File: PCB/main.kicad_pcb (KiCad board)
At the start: 4 copper layers, 65.2 x 45.1 mm, 64 parts, among them J1 S20B-PADSS-1, J2 S20B-PADSS-1, J3 SWD, SW1 SPST, U1 XC6206P33, U3 MCP2558FD, U4 MCP2558FD, U5 STM32G0B1, U6 TPS54302, Y1 40M

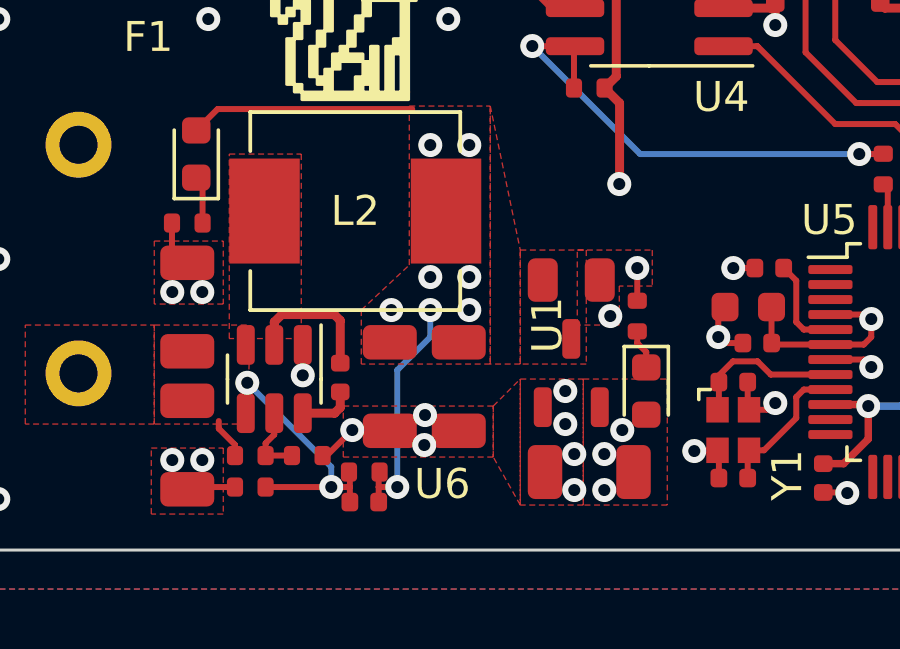
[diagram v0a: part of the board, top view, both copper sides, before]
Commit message: Switch to TJA1051T/3
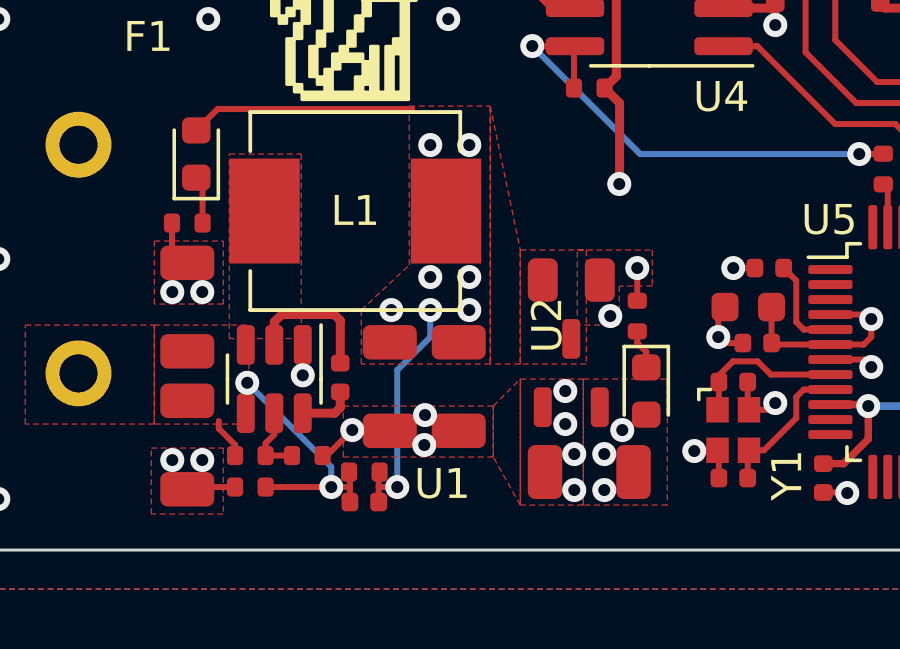
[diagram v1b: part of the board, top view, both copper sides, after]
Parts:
- U3, U4: value MCP2558FD -> TJA1051T/3
- renumbered C20 to C1, C11 to C10, C12 to C11, C13 to C12, C18 to C13, C17 to C14, C19 to C15, C14 to C16, C15 to C17, C16 to C18, C22 to C2, C23 to C3, C24 to C4, C25 to C5, C26 to C6, C1 to C7, C2 to C8, C10 to C9, D5 to D1, D1 to D2, D4 to D3, L2 to L1, R16 to R1, R8 to R10, R9 to R11, R10 to R12, R11 to R13, R13 to R14, R21 to R15, R22 to R16, R15 to R17, R17 to R18, R12 to R19, R18 to R2, R14 to R20, R25 to R21, R26 to R22, R27 to R25, R28 to R3, R20 to R4, R19 to R5, R1 to R6, R5 to R7, R6 to R8, R7 to R9, U6 to U1, U1 to U2

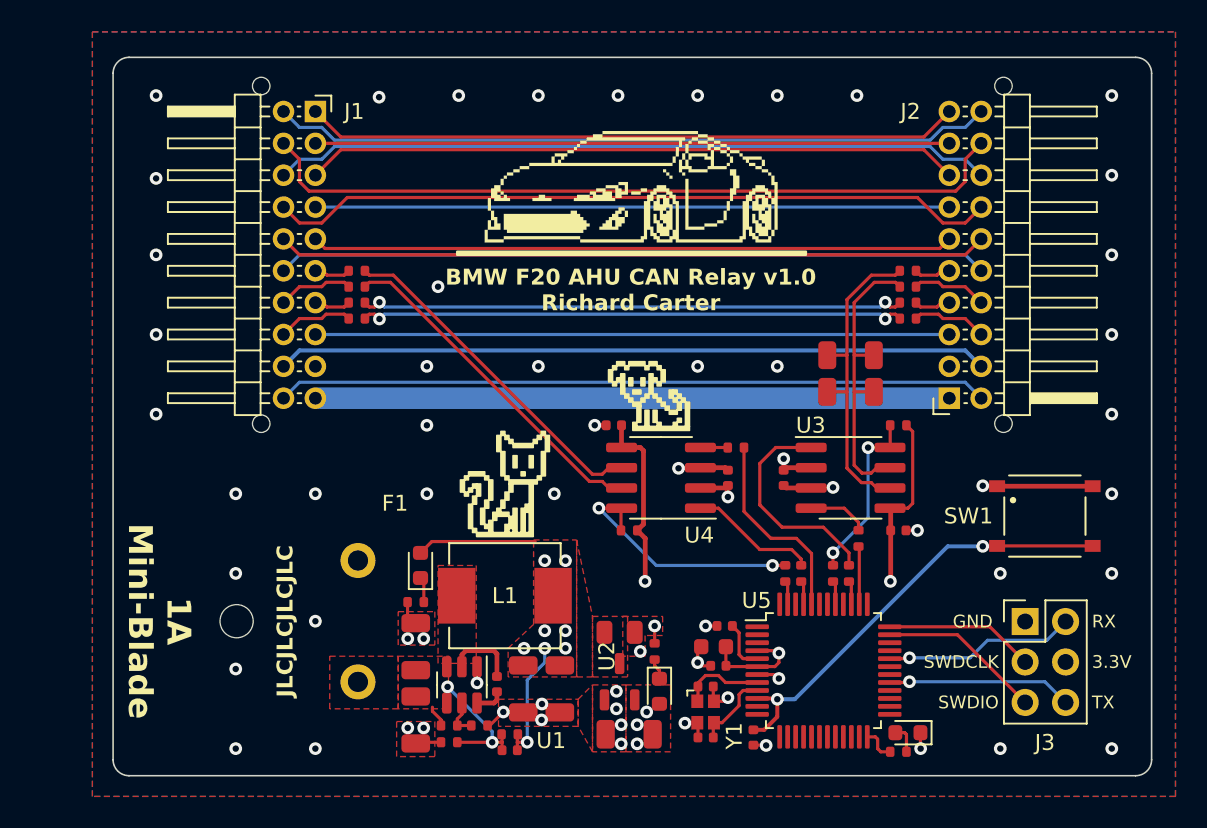
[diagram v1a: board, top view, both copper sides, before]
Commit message: Added bulk capacitance
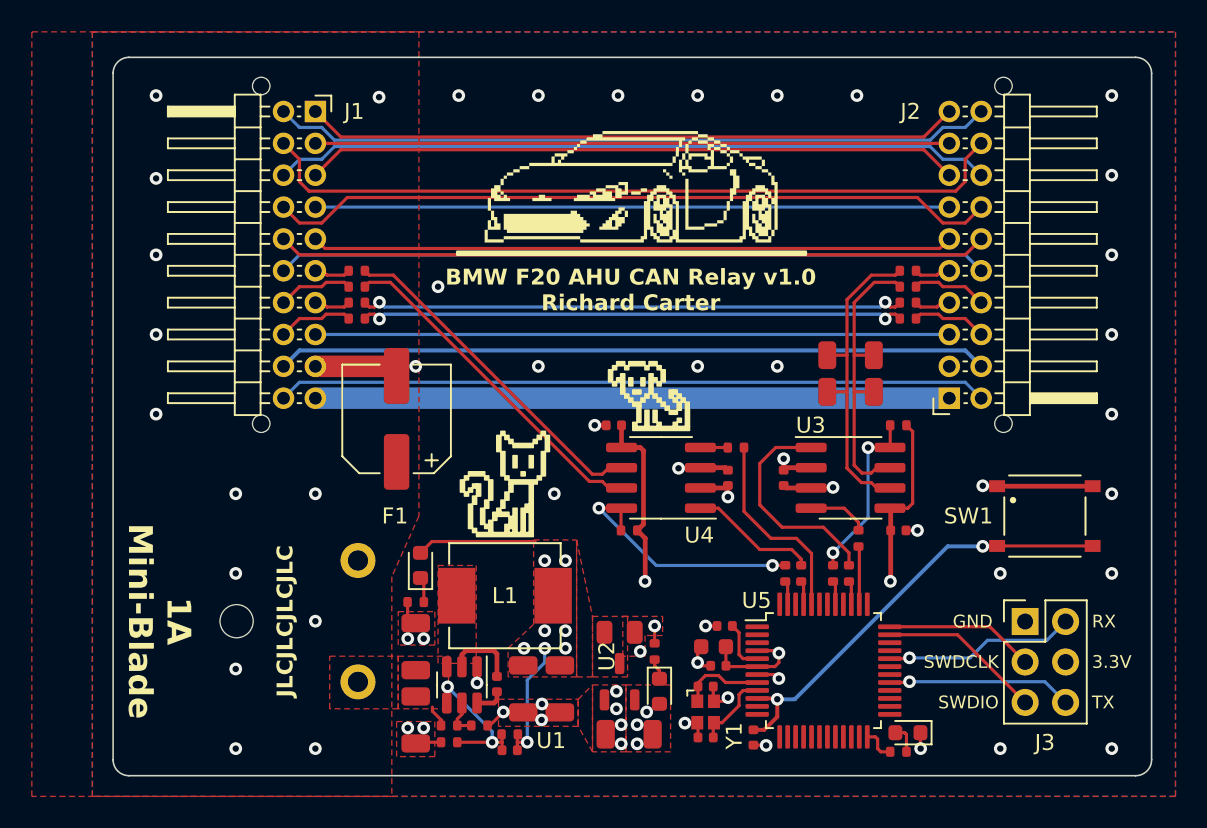
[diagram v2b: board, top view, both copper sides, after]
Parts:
- added C19: 47u, Capacitor_SMD:CP_Elec_6.3x5.8, F.Cu at (45.1, 49.3)
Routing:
- net GND: track 29.7 -> 34.9 mm, vias 63 -> 61
- added copper zone on F.Cu, net /JST_10_BAT+
- removed copper zone on In2.Cu, net /JST_10_BAT+
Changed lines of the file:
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@@
     )
   )
+  (footprint "Capacitor_SMD:CP_Elec_6.3x5.8" (layer "F.Cu")
+    (at 45.1 49.3 90)
+    (descr "SMD capacitor, aluminum electrolytic, Nichicon, 6.3x5.8mm")
+    (tags "capacitor electrolytic")
+    (property "Capacitance" "47u")
+    (property "Capacitance Tolerance" "20%")
+    (property "Case Package Size" "6.3x5.8 mm")
+    (property "Dielectric" "Aluminium")
+    (property "LCSC" "LCSC: C178545")
+    (property "MPN" "EEE-FK1E470P")
+    (property "Manufacturer" "Panasonic")
+    (property "Sheetfile" "main.kicad_sch")
+    (property "Sheetname" "")
+    (property "Voltage Rating" "25V")
+    (property "ki_description" "CAP ALUM 47UF 20% 25V SMD")
+    (property "ki_keywords" "cap capacitor")
+    (attr smd)
+    (fp_text reference "C19" (at 0 -4.35 90) (layer "F.SilkS") hide
+        (effects (font (size 1 1) (thickness 0.15)))
+    )
+    (fp_text value "47u" (at 0 4.35 90) (layer "F.Fab")
+        (effects (font (size 1 1) (thickness 0.15)))
+    )
+    (fp_text user "${REFERENCE}" (at 0 0 90) (layer "F.Fab")
+        (effects (font (size 1 1) (thickness 0.15)))
+    )
+    (fp_line (start -3.41 -2.345563) (end -3.41 -1.06)
+      (stroke (width 0.12) (type solid)) (layer "F.SilkS"))
+    (fp_line (start -3.41 -2.345563) (end -2.345563 -3.41)
+      (stroke (width 0.12) (type solid)) (layer "F.SilkS"))
+    (fp_line (start -3.41 2.345563) (end -3.41 1.06)
+      (stroke (width 0.12) (type solid)) (layer "F.SilkS"))
+    (fp_line (start -3.41 2.345563) (end -2.345563 3.41)
+      (stroke (width 0.12) (type solid)) (layer "F.SilkS"))
+    (fp_line (start -2.99375 2.2) (end -2.20625 2.2)
+      (stroke (width 0.12) (type solid)) (layer "F.SilkS"))
+    (fp_line (start -2.6 1.80625) (end -2.6 2.59375)
+      (stroke (width 0.12) (type solid)) (layer "F.SilkS"))
+    (fp_line (start -2.345563 -3.41) (end 3.41 -3.41)
+      (stroke (width 0.12) (type solid)) (layer "F.SilkS"))
+    (fp_line (start -2.345563 3.41) (end 3.41 3.41)
+      (stroke (width 0.12) (type solid)) (layer "F.SilkS"))
+    (fp_line (start 3.41 -3.41) (end 3.41 -1.06)
+      (stroke (width 0.12) (type solid)) (layer "F.SilkS"))
+    (fp_line (start 3.41 3.41) (end 3.41 1.06)
+      (stroke (width 0.12) (type solid)) (layer "F.SilkS"))
+    (fp_line (start -4.7 -1.05) (end -4.7 1.05)
+      (stroke (width 0.05) (type solid)) (layer "F.CrtYd"))
+    (fp_line (start -4.7 1.05) (end -3.55 1.05)
+      (stroke (width 0.05) (type solid)) (layer "F.CrtYd"))
+    (fp_line (start -3.55 -2.4) (end -3.55 -1.05)
+      (stroke (width 0.05) (type solid)) (layer "F.CrtYd"))
+    (fp_line (start -3.55 -2.4) (end -2.4 -3.55)
+      (stroke (width 0.05) (type solid)) (layer "F.CrtYd"))
+    (fp_line (start -3.55 -1.05) (end -4.7 -1.05)
+      (stroke (width 0.05) (type solid)) (layer "F.CrtYd"))
+    (fp_line (start -3.55 1.05) (end -3.55 2.4)
+      (stroke (width 0.05) (type solid)) (layer "F.CrtYd"))
+    (fp_line (start -3.55 2.4) (end -2.4 3.55)
+      (stroke (width 0.05) (type solid)) (layer "F.CrtYd"))
+    (fp_line (start -2.4 -3.55) (end 3.55 -3.55)
+      (stroke (width 0.05) (type solid)) (layer "F.CrtYd"))
+    (fp_line (start -2.4 3.55) (end 3.55 3.55)
+      (stroke (width 0.05) (type solid)) (layer "F.CrtYd"))
+    (fp_line (start 3.55 -3.55) (end 3.55 -1.05)
+      (stroke (width 0.05) (type solid)) (layer "F.CrtYd"))
+    (fp_line (start 3.55 -1.05) (end 4.7 -1.05)
+      (stroke (width 0.05) (type solid)) (layer "F.CrtYd"))
+    (fp_line (start 3.55 1.05) (end 3.55 3.55)
+      (stroke (width 0.05) (type solid)) (layer "F.CrtYd"))
+    (fp_line (start 4.7 -1.05) (end 4.7 1.05)
+      (stroke (width 0.05) (type solid)) (layer "F.CrtYd"))
+    (fp_line (start 4.7 1.05) (end 3.55 1.05)
+      (stroke (width 0.05) (type solid)) (layer "F.CrtYd"))
+    (fp_line (start -3.3 -2.3) (end -3.3 2.3)
+      (stroke (width 0.1) (type solid)) (layer "F.Fab"))
+    (fp_line (start -3.3 -2.3) (end -2.3 -3.3)
+      (stroke (width 0.1) (type solid)) (layer "F.Fab"))
+    (fp_line (start -3.3 2.3) (end -2.3 3.3)
+      (stroke (width 0.1) (type solid)) (layer "F.Fab"))
+    (fp_line (start -2.704838 -1.33) (end -2.074838 -1.33)
+      (stroke (width 0.1) (type solid)) (layer "F.Fab"))
+    (fp_line (start -2.389838 -1.645) (end -2.389838 -1.015)
+      (stroke (width 0.1) (type solid)) (layer "F.Fab"))
+    (fp_line (start -2.3 -3.3) (end 3.3 -3.3)
+      (stroke (width 0.1) (type solid)) (layer "F.Fab"))
+    (fp_line (start -2.3 3.3) (end 3.3 3.3)
+      (stroke (width 0.1) (type solid)) (layer "F.Fab"))
+    (fp_line (start 3.3 -3.3) (end 3.3 3.3)
+      (stroke (width 0.1) (type solid)) (layer "F.Fab"))
+    (fp_circle (center 0 0) (end 3.15 0)
+      (stroke (width 0.1) (type solid)) (fill none) (layer "F.Fab"))
+    (pad "1" smd roundrect (at -2.7 0 90) (size 3.5 1.6) (layers "F.Cu" "F.Paste" "F.Mask") (roundrect_rratio 0.15625)
+      (net 61 "/JST_10_BAT+") (pintype "passive"))
+    (pad "2" smd roundrect (at 2.7 0 90) (size 3.5 1.6) (layers "F.Cu" "F.Paste" "F.Mask") (roundrect_rratio 0.15625)
+      (net 81 "GND") (pintype "passive"))
+    (model "${KICAD6_3DMODEL_DIR}/Capacitor_SMD.3dshapes/CP_Elec_6.3x5.8.wrl"
+      (offset (xyz 0 0 0))
+      (scale (xyz 1 1 1))
+      (rotate (xyz 0 0 0))
+    )
+  )
   (footprint "Resistor_SMD:R_0402_1005Metric" (layer "F.Cu")
     (at 42.6 40 180)
@@
     (property "ki_keywords" "fuse")
     (attr through_hole)
-    (fp_text reference "F1" (at -7.4 -9.9451) (layer "F.SilkS")
+    (fp_text reference "F1" (at -6.6 -9.9451) (layer "F.SilkS")
         (effects (font (size 1 1) (thickness 0.15)))
     )
@@
   (segment (start 65.22 62.3) (end 64.5 62.3) (width 0.2) (layer "F.Cu") (net 81))
   (segment (start 64.2 64.8) (end 64 64.6) (width 0.2) (layer "F.Cu") (net 81))
+  (segment (start 40 46) (end 45.2 46) (width 1.35) (layer "F.Cu") (net 81))
   (segment (start 69.4 52.52) (end 69.4 51.8) (width 0.3) (layer "F.Cu") (net 81))
   (segment (start 47.89 69.6) (end 46.625 69.6) (width 0.2) (layer "F.Cu") (net 81))
@@
   (via (at 78 70) (size 0.8) (drill 0.4) (layers "F.Cu" "B.Cu") (net 81))
   (via (at 90 44) (size 0.8) (drill 0.4) (layers "F.Cu" "B.Cu") (net 81))
-  (via (at 47 46) (size 0.8) (drill 0.4) (layers "F.Cu" "B.Cu") (net 81))
   (via (at 55 54) (size 0.8) (drill 0.4) (layers "F.Cu" "B.Cu") (free) (net 81))
   (via (at 47.7 41) (size 0.8) (drill 0.4) (layers "F.Cu" "B.Cu") (net 81))
@@
   (via (at 83 59) (size 0.8) (drill 0.4) (layers "F.Cu" "B.Cu") (free) (net 81))
   (via (at 35 59) (size 0.8) (drill 0.4) (layers "F.Cu" "B.Cu") (free) (net 81))
-  (via (at 47 49.7) (size 0.8) (drill 0.4) (layers "F.Cu" "B.Cu") (net 81))
   (via (at 69.1 65.599503) (size 0.8) (drill 0.4) (layers "F.Cu" "B.Cu") (net 81))
   (via (at 68.3 69.7995) (size 0.8) (drill 0.4) (layers "F.Cu" "B.Cu") (net 81))
@@
   (via (at 30 44) (size 0.8) (drill 0.4) (layers "F.Cu" "B.Cu") (net 81))
   (via (at 77.8 56.3) (size 0.8) (drill 0.4) (layers "F.Cu" "B.Cu") (net 81))
+  (via (at 46.3 46) (size 0.8) (drill 0.4) (layers "F.Cu" "B.Cu") (free) (net 81))
   (via (at 74 29) (size 0.8) (drill 0.4) (layers "F.Cu" "B.Cu") (net 81))
   (via (at 90 54) (size 0.8) (drill 0.4) (layers "F.Cu" "B.Cu") (free) (net 81))
@@
   (via (at 69.4 51.8) (size 0.8) (drill 0.4) (layers "F.Cu" "B.Cu") (net 81))
   (via (at 59.2 69.7) (size 0.8) (drill 0.4) (layers "F.Cu" "B.Cu") (free) (net 81))
-  (via (at 47 54) (size 0.8) (drill 0.4) (layers "F.Cu" "B.Cu") (free) (net 81))
   (via (at 44 29.1) (size 0.8) (drill 0.4) (layers "F.Cu" "B.Cu") (net 81))
   (via (at 58.9 67.5) (size 0.8) (drill 0.4) (layers "F.Cu" "B.Cu") (free) (net 81))
@@
     )
   )
+  (zone (net 61) (net_name "/JST_10_BAT+") (layer "F.Cu") (hatch edge 0.5)
+    (priority 5)
+    (connect_pads yes (clearance 0.5))
+    (min_thickness 0.25) (filled_areas_thickness no)
+    (fill yes (thermal_gap 0.5) (thermal_bridge_width 0.5))
+    (polygon
+      (pts
+        (xy 46.5 55.4)
+        (xy 44.8 59.2)
+        (xy 44.8 73)
+        (xy 22.2 73)
+        (xy 22.2 25)
+        (xy 46.5 25)
+      )
+    )
+  )
   (zone (net 81) (net_name "GND") (layers "F.Cu" "In1.Cu" "In2.Cu" "B.Cu") (hatch edge 0.5)
     (connect_pads yes (clearance 0.5))
@@
     (polygon
       (pts
-        (xy 44.7 49)
+        (xy 44.7 49.1)
         (xy 92.2 49.1)
         (xy 92.2 71)
@@
       )
     )
-  )
-  (zone (net 61) (net_name "/JST_10_BAT+") (layer "In2.Cu") (hatch edge 0.5)
-    (priority 5)
-    (connect_pads yes (clearance 0.5))
-    (min_thickness 0.25) (filled_areas_thickness no)
-    (fill yes (thermal_gap 0.5) (thermal_bridge_width 0.5))
-    (polygon
-      (pts
-        (xy 44.7 3.5)
-        (xy 44.7 92.8)
-        (xy -5.2 92.8)
-        (xy -5.2 3.5)
-      )
-    )

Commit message: Generate output files
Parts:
- C13, C14: value 15p -> 27p
- Y1: footprint libdb:CMP-0004 -> Crystal:Crystal_SMD_3225-4Pin_3.2x2.5mm
- moved C13 2.33 mm to (62.8, 67.7), turned to -90 degrees
- moved C14 0.98 mm to (64.9, 70.2)
- moved Y1 0.40 mm to (64.9, 67.7)
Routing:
- net GND: track 34.9 -> 37.2 mm
- net /XTAL1: track 5.26 -> 5.92 mm

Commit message: Change switch
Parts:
- SW1: value SPST -> Tactile; footprint libdb:CMP-0011 -> libdb:CMP-0072
- moved SW1 0.10 mm to (85.8, 55.5), turned to 180 degrees
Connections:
- SW1 pad 1: GND -> Net-(U5-PF2)
- SW1 pad 2: Net-(U5-PF2) -> GND
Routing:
- net GND: track 37.2 -> 30.3 mm, vias 61 -> 59
- net Net-(U5-PF2): track 28.0 -> 27.4 mm

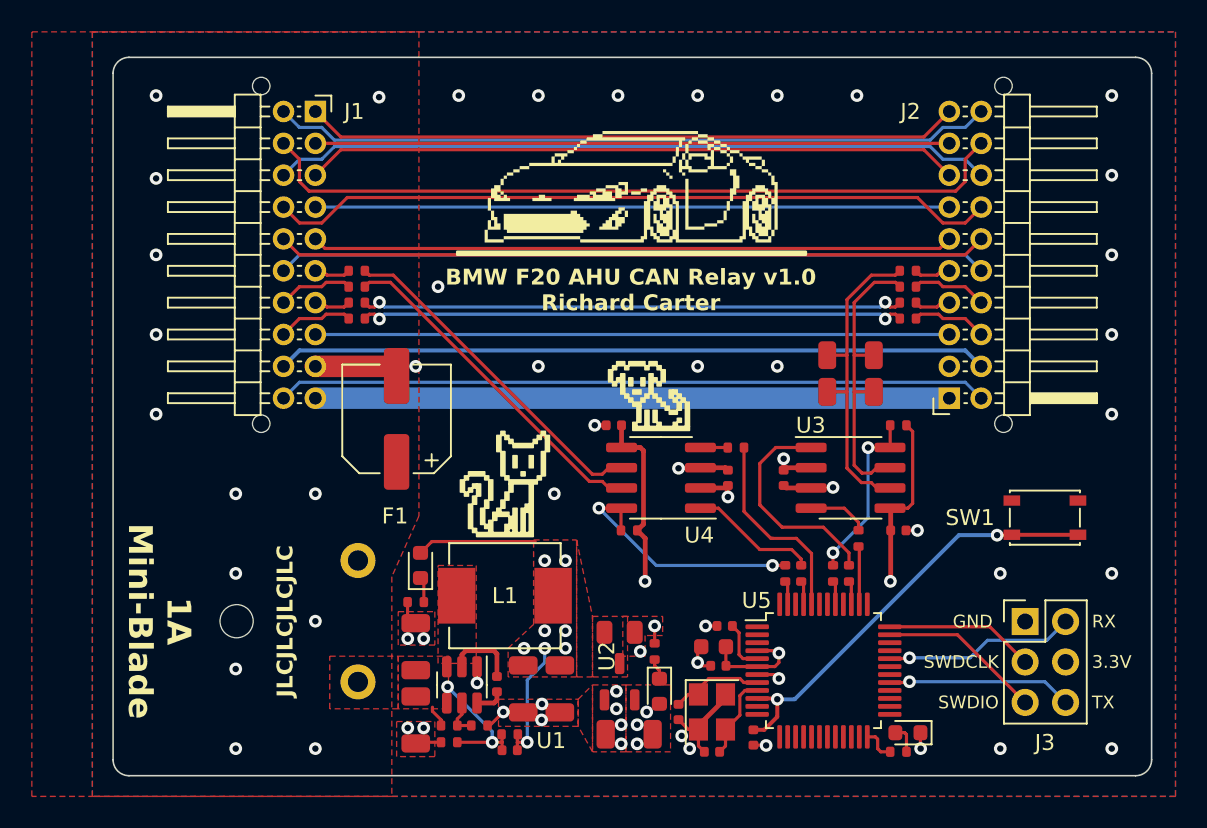
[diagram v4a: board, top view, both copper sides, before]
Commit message: Redo layout to support use of B20B-PADSS due to stock inavailability
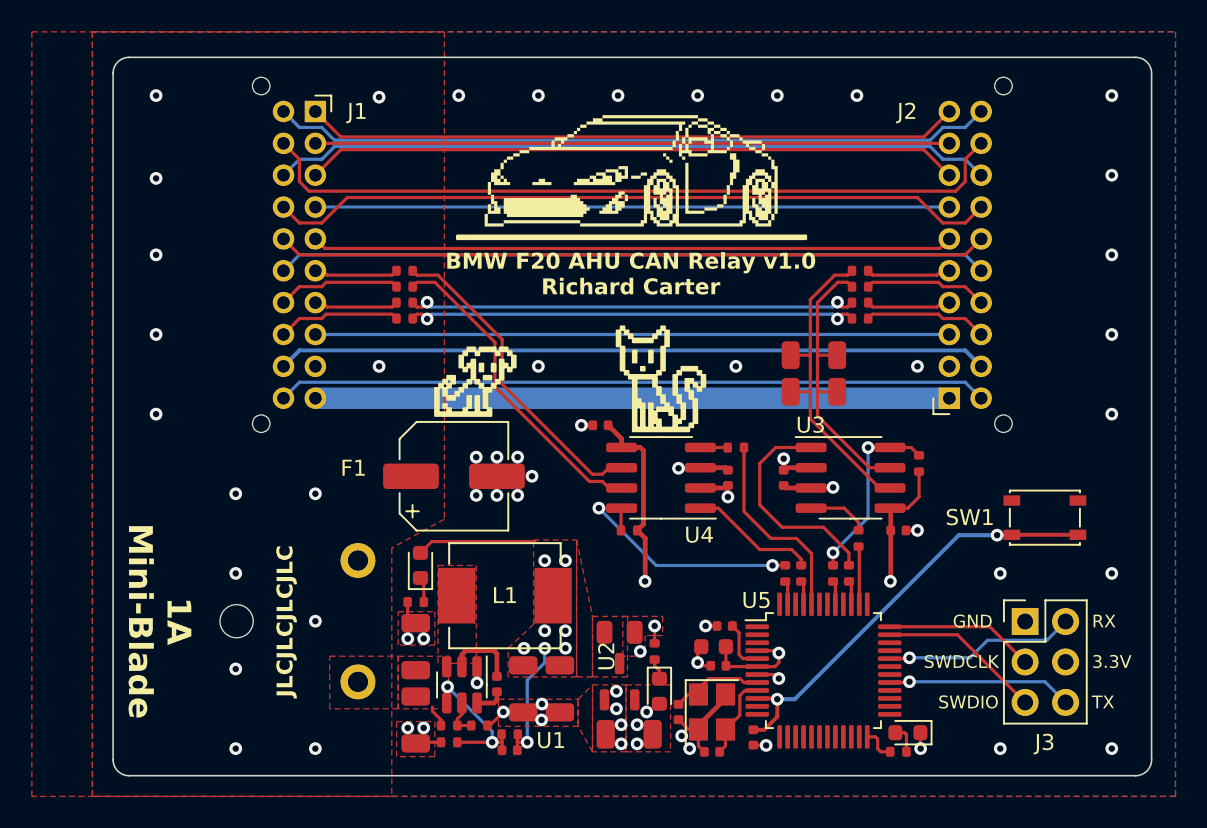
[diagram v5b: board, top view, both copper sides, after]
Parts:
- removed ART1: Cat (small, mirrored), libdb:CMP-0044
- removed ART2: Dog (small), libdb:CMP-0045
- added REF**: CMP-0043, libdb:CMP-0043, F.Cu at (61.7, 47.8)
- added REF**: CMP-0075, libdb:CMP-0075, F.Cu at (50.3, 47.6)
- moved C19 5.09 mm to (48.7, 52.9), turned to 0 degrees
- moved R13 3.00 mm to (45.6, 41.0)
- moved R14 3.00 mm to (45.6, 40.0)
- moved R15 3.00 mm to (45.6, 43.0)
- moved R16 3.00 mm to (45.6, 42.0)
- moved R17 3.00 mm to (74.2, 41.0)
- moved R18 3.00 mm to (74.2, 40.0)
- moved R19 3.00 mm to (74.2, 43.0)
- moved R20 3.00 mm to (74.2, 42.0)
- moved R10 2.73 mm to (77.9, 52.1), turned to -90 degrees
- moved R7 2.30 mm to (71.3, 45.3)
- moved R8 2.30 mm to (71.3, 47.6)
- moved REF** 1.00 mm to (50.6, 30.2)
- moved C11 0.84 mm to (57.9, 49.7)
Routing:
- net /FW_CAN2-: track 34.3 -> 28.3 mm
- net /FW_CAN2+: track 34.3 -> 28.3 mm
- net GND: track 30.3 -> 25.1 mm, vias 59 -> 64
- net /NC_CAN2-: track 2.32 -> 5.32 mm
- net /NC_CAN2+: track 4.73 -> 7.73 mm
- net /IN_NC_CAN2-: track 2.32 -> 5.32 mm
- net /IN_NC_CAN2+: track 4.73 -> 7.73 mm
- net /IN_CAN1-: track 2.32 -> 5.32 mm
- net /IN_CAN1+: track 4.73 -> 7.73 mm
- net /CAN1-: track 2.32 -> 5.32 mm
- net /CAN1+: track 4.73 -> 7.73 mm
- net +3.3V: track 29.3 -> 26.8 mm
- net /Relay_IN_CAN-: track 21.6 -> 20.2 mm
- net /Relay_IN_CAN+: track 21.6 -> 20.2 mm
- net /FDCAN1_S: track 11.1 -> 11.7 mm
